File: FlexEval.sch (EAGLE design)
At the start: 173 parts, among them J1 USB4105-GF-A, J2 GRPB052VWQS-RC, SW1 1825910-7, U1 MK22FX512AVLQ12, U3 IS31FL3733B-TQLS4, U4 IS31FL3733B-TQLS4, U5 SOIC127P600X175-8N, U6 AP2115M-3.3TRG1, Y1 ABM3B-8.000MHZ-B2-T, Y2 ABS07-32.768KHZ-T

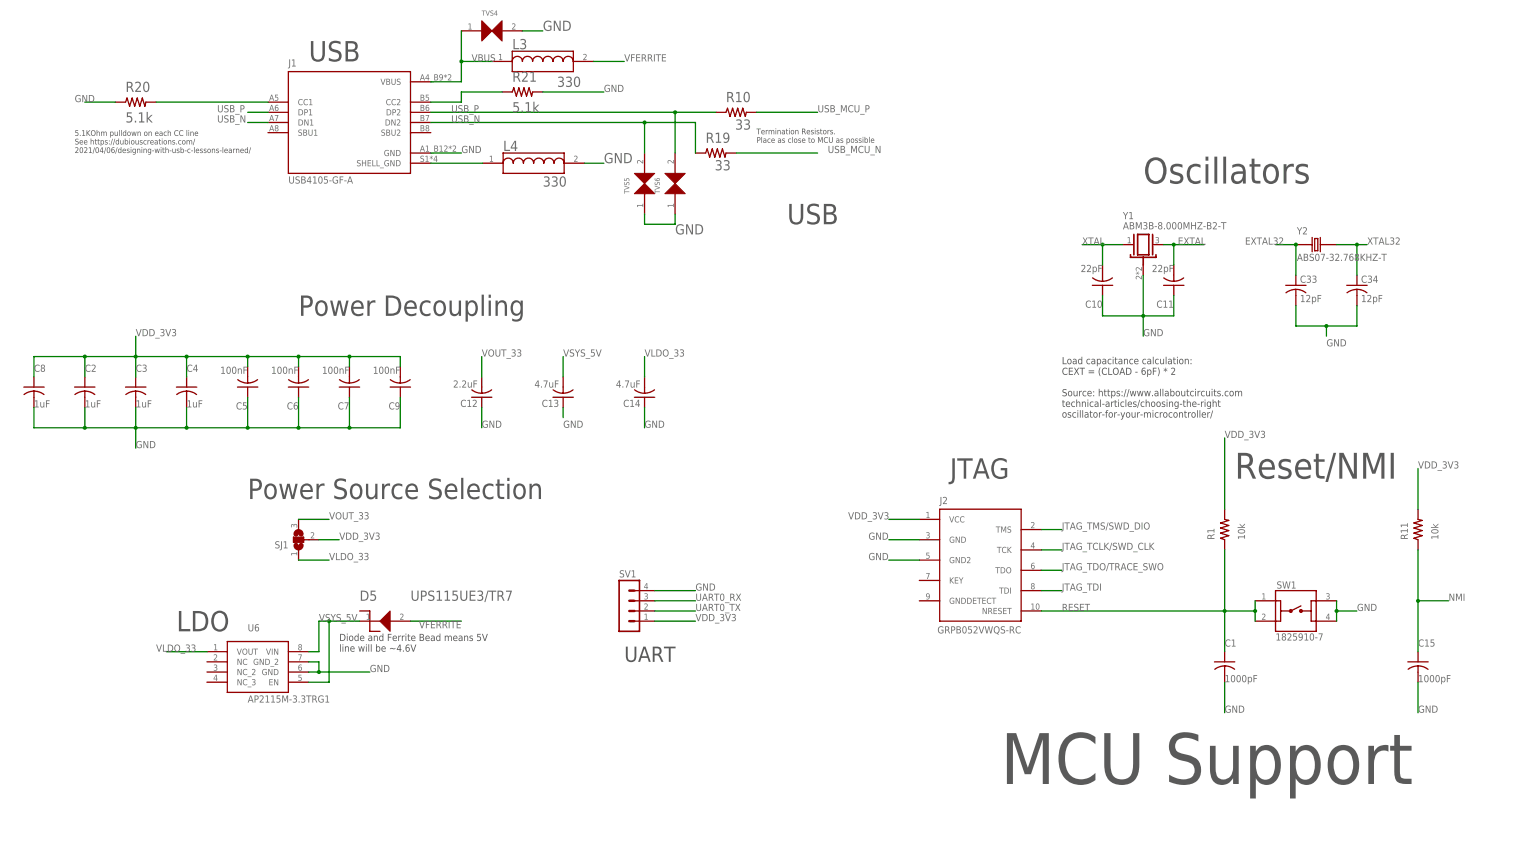
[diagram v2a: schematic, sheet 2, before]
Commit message: board: added test points and debug LEDs
Added two debug LEDs, and test points on I2C and voltage signals. BOM
updated with 2 additional 200 Ohm resistors and 2 1206 LEDs

Signed-off-by: Daniel DeGrasse <daniel@degrasse.com>
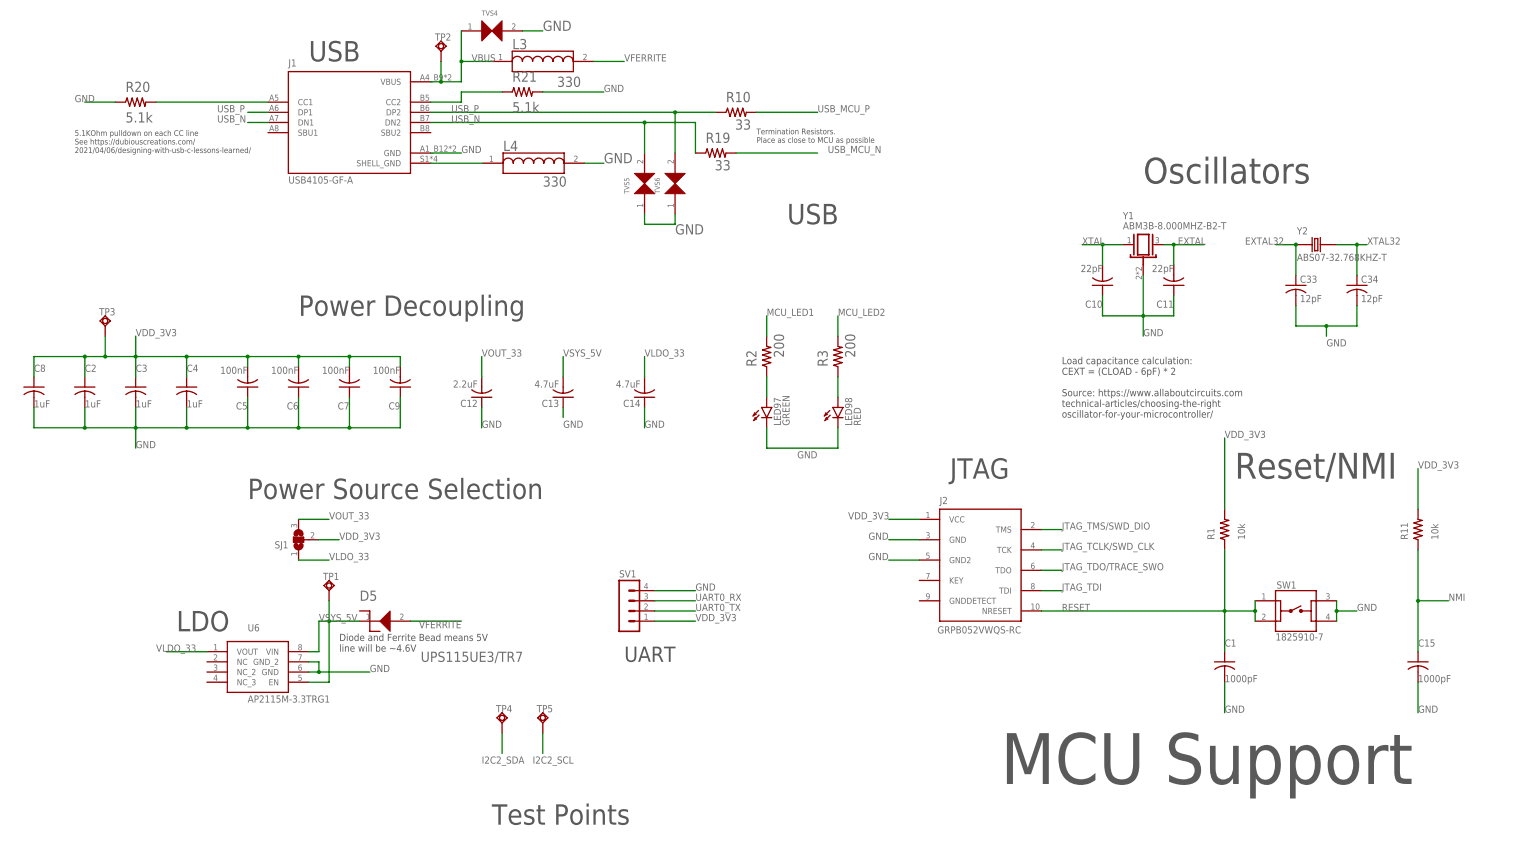
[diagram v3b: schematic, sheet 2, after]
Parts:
- added LED97: GREEN, led:LEDSML1206
- added LED98: RED, led:LEDSML1206
- added R2, R3: 200, resistor:R-US_R0805
- added TP1, TP2, TP3, TP4, TP5: TPSQTP20R, testpad:TPSQTP20R
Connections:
- new net MCU_LED1: R2.2, U1A.PTE24
- new net MCU_LED2: R3.2, U1A.PTE25
- new net N$1: LED97.A, R2.1
- new net N$2: LED98.A, R3.1
- net GND: now also LED97.C, LED98.C
- net I2C2_SCL: now also TP5.TP
- net I2C2_SDA: now also TP4.TP
- net VBUS: now also TP2.TP
- net VDD_3V3: now also TP3.TP
- net VSYS_5V: now also TP1.TP
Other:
- note added: "Test Points"
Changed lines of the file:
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@@
 <part name="C33" library="resistor" library_urn="urn:adsk.eagle:library:348" deviceset="C-US" device="C0805" package3d_urn="urn:adsk.eagle:package:23617/2" value="12pF"/>
 <part name="C34" library="resistor" library_urn="urn:adsk.eagle:library:348" deviceset="C-US" device="C0805" package3d_urn="urn:adsk.eagle:package:23617/2" value="12pF"/>
+<part name="LED97" library="led" library_urn="urn:adsk.eagle:library:259" deviceset="LED" device="SML1206" package3d_urn="urn:adsk.eagle:package:15829/1" value="GREEN"/>
+<part name="LED98" library="led" library_urn="urn:adsk.eagle:library:259" deviceset="LED" device="SML1206" package3d_urn="urn:adsk.eagle:package:15829/1" value="RED"/>
+<part name="R2" library="resistor" library_urn="urn:adsk.eagle:library:348" deviceset="R-US_" device="R0805" package3d_urn="urn:adsk.eagle:package:23553/2" value="200"/>
+<part name="R3" library="resistor" library_urn="urn:adsk.eagle:library:348" deviceset="R-US_" device="R0805" package3d_urn="urn:adsk.eagle:package:23553/2" value="200"/>
+<part name="TP1" library="testpad" library_urn="urn:adsk.eagle:library:385" deviceset="TPSQ" device="TP20R" package3d_urn="urn:adsk.eagle:package:27973/1"/>
+<part name="TP2" library="testpad" library_urn="urn:adsk.eagle:library:385" deviceset="TPSQ" device="TP20R" package3d_urn="urn:adsk.eagle:package:27973/1"/>
+<part name="TP3" library="testpad" library_urn="urn:adsk.eagle:library:385" deviceset="TPSQ" device="TP20R" package3d_urn="urn:adsk.eagle:package:27973/1"/>
+<part name="TP4" library="testpad" library_urn="urn:adsk.eagle:library:385" deviceset="TPSQ" device="TP20R" package3d_urn="urn:adsk.eagle:package:27973/1"/>
+<part name="TP5" library="testpad" library_urn="urn:adsk.eagle:library:385" deviceset="TPSQ" device="TP20R" package3d_urn="urn:adsk.eagle:package:27973/1"/>
 </parts>
 <sheets>
@@
 <wire x1="-86.36" y1="83.82" x2="-96.52" y2="83.82" width="0.1524" layer="91"/>
 <label x="-109.22" y="83.82" size="1.778" layer="95"/>
+</segment>
+</net>
+<net name="MCU_LED1" class="0">
+<segment>
+<pinref part="U1" gate="A" pin="PTE24"/>
+<wire x1="96.52" y1="40.64" x2="106.68" y2="40.64" width="0.1524" layer="91"/>
+<label x="106.68" y="40.64" size="1.778" layer="95"/>
+</segment>
+</net>
+<net name="MCU_LED2" class="0">
+<segment>
+<pinref part="U1" gate="A" pin="PTE25"/>
+<wire x1="96.52" y1="43.18" x2="106.68" y2="43.18" width="0.1524" layer="91"/>
+<label x="106.68" y="43.18" size="1.778" layer="95"/>
 </segment>
 </net>
@@
 <text x="30.48" y="86.36" size="1.4224" layer="97">Termination Resistors.
 Place as close to MCU as possible</text>
+<text x="-35.56" y="-83.82" size="5.08" layer="97">Test Points</text>
 </plain>
 <instances>
@@
 <instance part="D5" gate="G$1" x="-63.5" y="-33.02" smashed="yes">
 <attribute name="NAME" x="-68.58" y="-27.94" size="2.54" layer="95"/>
-<attribute name="VALUE" x="-55.88" y="-27.94" size="2.54" layer="96"/>
+<attribute name="VALUE" x="-53.34" y="-43.18" size="2.54" layer="96"/>
 </instance>
 <instance part="R11" gate="G$1" x="195.58" y="-10.16" smashed="yes" rot="R90">
@@
 <attribute name="NAME" x="181.356" y="51.435" size="1.778" layer="95"/>
 <attribute name="VALUE" x="181.356" y="46.609" size="1.778" layer="96"/>
+</instance>
+<instance part="LED97" gate="G$1" x="33.02" y="20.32" smashed="yes">
+<attribute name="NAME" x="36.576" y="15.748" size="1.778" layer="95" rot="R90"/>
+<attribute name="VALUE" x="38.735" y="15.748" size="1.778" layer="96" rot="R90"/>
+</instance>
+<instance part="LED98" gate="G$1" x="50.8" y="20.32" smashed="yes">
+<attribute name="NAME" x="54.356" y="15.748" size="1.778" layer="95" rot="R90"/>
+<attribute name="VALUE" x="56.515" y="15.748" size="1.778" layer="96" rot="R90"/>
+</instance>
+<instance part="R2" gate="G$1" x="33.02" y="33.02" smashed="yes" rot="R90">
+<attribute name="NAME" x="30.47851875" y="30.475559375" size="2.54148125" layer="95" rot="R90"/>
+<attribute name="VALUE" x="37.344640625" y="32.75603125" size="2.54331875" layer="96" rot="R90"/>
+</instance>
+<instance part="R3" gate="G$1" x="50.8" y="33.02" smashed="yes" rot="R90">
+<attribute name="NAME" x="48.25851875" y="30.475559375" size="2.54148125" layer="95" rot="R90"/>
+<attribute name="VALUE" x="55.124640625" y="32.75603125" size="2.54331875" layer="96" rot="R90"/>
+</instance>
+<instance part="TP1" gate="G$1" x="-76.2" y="-25.4" smashed="yes" rot="R180">
+<attribute name="NAME" x="-73.66" y="-20.955" size="1.778" layer="95" rot="R180"/>
+<attribute name="TP_SIGNAL_NAME" x="-78.74" y="-24.13" size="1.778" layer="97" rot="R180"/>
+</instance>
+<instance part="TP2" gate="G$1" x="-48.26" y="109.22" smashed="yes" rot="R180">
+<attribute name="NAME" x="-45.72" y="113.665" size="1.778" layer="95" rot="R180"/>
+<attribute name="TP_SIGNAL_NAME" x="-50.8" y="110.49" size="1.778" layer="97" rot="R180"/>
+</instance>
+<instance part="TP3" gate="G$1" x="-132.08" y="40.64" smashed="yes" rot="R180">
+<attribute name="NAME" x="-129.54" y="45.085" size="1.778" layer="95" rot="R180"/>
+<attribute name="TP_SIGNAL_NAME" x="-134.62" y="41.91" size="1.778" layer="97" rot="R180"/>
+</instance>
+<instance part="TP4" gate="G$1" x="-33.02" y="-58.42" smashed="yes" rot="R180">
+<attribute name="NAME" x="-30.48" y="-53.975" size="1.778" layer="95" rot="R180"/>
+<attribute name="TP_SIGNAL_NAME" x="-35.56" y="-57.15" size="1.778" layer="97" rot="R180"/>
+</instance>
+<instance part="TP5" gate="G$1" x="-22.86" y="-58.42" smashed="yes" rot="R180">
+<attribute name="NAME" x="-20.32" y="-53.975" size="1.778" layer="95" rot="R180"/>
+<attribute name="TP_SIGNAL_NAME" x="-25.4" y="-57.15" size="1.778" layer="97" rot="R180"/>
 </instance>
 </instances>
@@
 <pinref part="C2" gate="G$1" pin="1"/>
 <wire x1="-137.16" y1="27.94" x2="-137.16" y2="33.02" width="0.1524" layer="91"/>
-<wire x1="-137.16" y1="33.02" x2="-124.46" y2="33.02" width="0.1524" layer="91"/>
+<wire x1="-137.16" y1="33.02" x2="-132.08" y2="33.02" width="0.1524" layer="91"/>
 <pinref part="C4" gate="G$1" pin="1"/>
+<wire x1="-132.08" y1="33.02" x2="-124.46" y2="33.02" width="0.1524" layer="91"/>
 <wire x1="-124.46" y1="33.02" x2="-111.76" y2="33.02" width="0.1524" layer="91"/>
 <wire x1="-111.76" y1="33.02" x2="-111.76" y2="27.94" width="0.1524" layer="91"/>
@@
 <pinref part="C9" gate="G$1" pin="2"/>
 <wire x1="-58.42" y1="33.02" x2="-58.42" y2="30.48" width="0.1524" layer="91"/>
+<pinref part="TP3" gate="G$1" pin="TP"/>
+<wire x1="-132.08" y1="38.1" x2="-132.08" y2="33.02" width="0.1524" layer="91"/>
+<junction x="-132.08" y="33.02"/>
 </segment>
 <segment>
@@
 <label x="172.72" y="35.56" size="1.778" layer="95"/>
 </segment>
+<segment>
+<pinref part="LED97" gate="G$1" pin="C"/>
+<wire x1="33.02" y1="15.24" x2="33.02" y2="10.16" width="0.1524" layer="91"/>
+<wire x1="33.02" y1="10.16" x2="50.8" y2="10.16" width="0.1524" layer="91"/>
+<pinref part="LED98" gate="G$1" pin="C"/>
+<wire x1="50.8" y1="10.16" x2="50.8" y2="15.24" width="0.1524" layer="91"/>
+<label x="40.64" y="7.62" size="1.778" layer="95"/>
+</segment>
 </net>
 <net name="JTAG_TCLK/SWD_CLK" class="0">
@@
 <wire x1="-43.18" y1="106.68" x2="-35.56" y2="106.68" width="0.1524" layer="91"/>
 <wire x1="-43.18" y1="114.3" x2="-43.18" y2="106.68" width="0.1524" layer="91"/>
-<wire x1="-50.8" y1="101.6" x2="-43.18" y2="101.6" width="0.1524" layer="91"/>
+<wire x1="-50.8" y1="101.6" x2="-48.26" y2="101.6" width="0.1524" layer="91"/>
+<wire x1="-48.26" y1="101.6" x2="-43.18" y2="101.6" width="0.1524" layer="91"/>
 <wire x1="-43.18" y1="101.6" x2="-43.18" y2="106.68" width="0.1524" layer="91"/>
 <junction x="-43.18" y="106.68"/>
@@
 <pinref part="L3" gate="G$1" pin="1"/>
 <pinref part="TVS4" gate="G$1" pin="1"/>
+<pinref part="TP2" gate="G$1" pin="TP"/>
+<wire x1="-48.26" y1="106.68" x2="-48.26" y2="101.6" width="0.1524" layer="91"/>
+<junction x="-48.26" y="101.6"/>
 </segment>
 </net>
@@
 <wire x1="-76.2" y1="-48.26" x2="-81.28" y2="-48.26" width="0.1524" layer="91"/>
 <label x="-78.74" y="-33.02" size="1.778" layer="95"/>
+<pinref part="TP1" gate="G$1" pin="TP"/>
+<wire x1="-76.2" y1="-27.94" x2="-76.2" y2="-33.02" width="0.1524" layer="91"/>
 </segment>
 </net>
@@
 </segment>
 <segment>
-<wire x1="-55.88" y1="-33.02" x2="-43.18" y2="-33.02" width="0.1524" layer="91"/>
 <label x="-43.18" y="-33.02" size="1.778" layer="95" rot="R180"/>
 <pinref part="D5" gate="G$1" pin="P$2"/>
-</segment>
-</net>
+<wire x1="-55.88" y1="-33.02" x2="-43.18" y2="-33.02" width="0.1524" layer="91"/>
+</segment>
+</net>
+<net name="N$1" class="0">
+<segment>
+<pinref part="R2" gate="G$1" pin="1"/>
+<pinref part="LED97" gate="G$1" pin="A"/>
+<wire x1="33.02" y1="27.94" x2="33.02" y2="22.86" width="0.1524" layer="91"/>
+</segment>
+</net>
+<net name="N$2" class="0">
+<segment>
+<pinref part="R3" gate="G$1" pin="1"/>
+<pinref part="LED98" gate="G$1" pin="A"/>
+<wire x1="50.8" y1="27.94" x2="50.8" y2="22.86" width="0.1524" layer="91"/>
+</segment>
+</net>
+<net name="MCU_LED1" class="0">
+<segment>
+<pinref part="R2" gate="G$1" pin="2"/>
+<wire x1="33.02" y1="38.1" x2="33.02" y2="43.18" width="0.1524" layer="91"/>
+<label x="33.02" y="43.18" size="1.778" layer="95"/>
+</segment>
+</net>
+<net name="MCU_LED2" class="0">
+<segment>
+<pinref part="R3" gate="G$1" pin="2"/>
+<wire x1="50.8" y1="38.1" x2="50.8" y2="43.18" width="0.1524" layer="91"/>
+<label x="50.8" y="43.18" size="1.778" layer="95"/>
+</segment>
+</net>
+<net name="I2C2_SDA" class="0">
+<segment>
+<pinref part="TP4" gate="G$1" pin="TP"/>
+<wire x1="-33.02" y1="-60.96" x2="-33.02" y2="-66.04" width="0.1524" layer="91"/>
+<label x="-38.1" y="-68.58" size="1.778" layer="95"/>
+</segment>
+</net>
+<net name="I2C2_SCL" class="0">
+<segment>
+<pinref part="TP5" gate="G$1" pin="TP"/>
+<wire x1="-22.86" y1="-60.96" x2="-22.86" y2="-66.04" width="0.1524" layer="91"/>
+<label x="-25.4" y="-68.58" size="1.778" layer="95"/>
+</segment>
+</net>
